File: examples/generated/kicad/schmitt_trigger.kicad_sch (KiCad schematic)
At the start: 6 parts

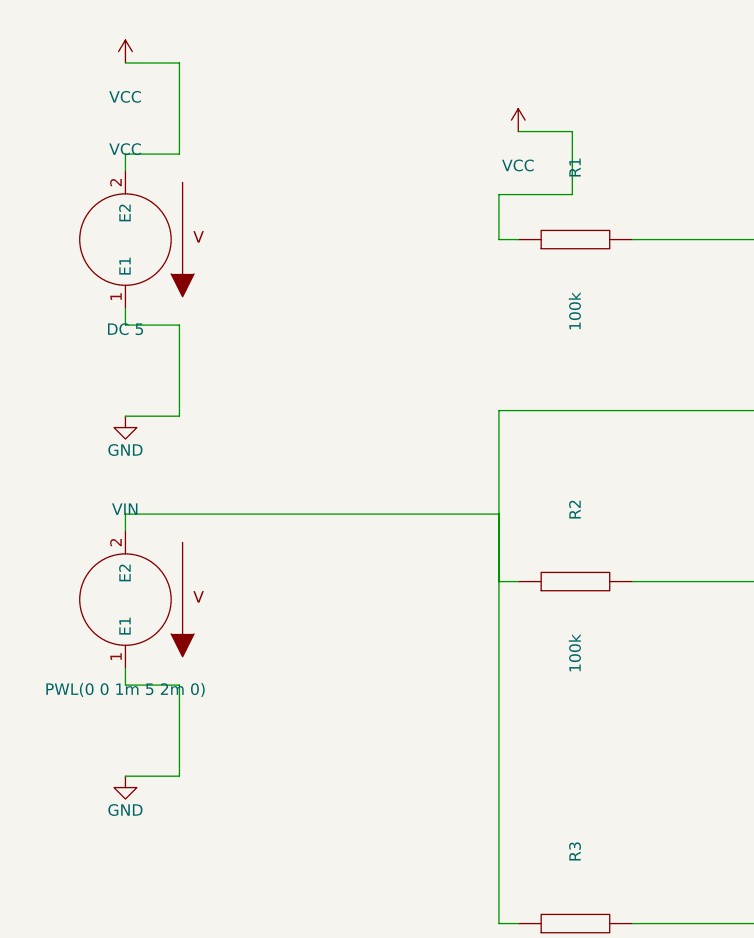
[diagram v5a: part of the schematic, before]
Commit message: Attempt to fix kinking and terminal direction issuses.
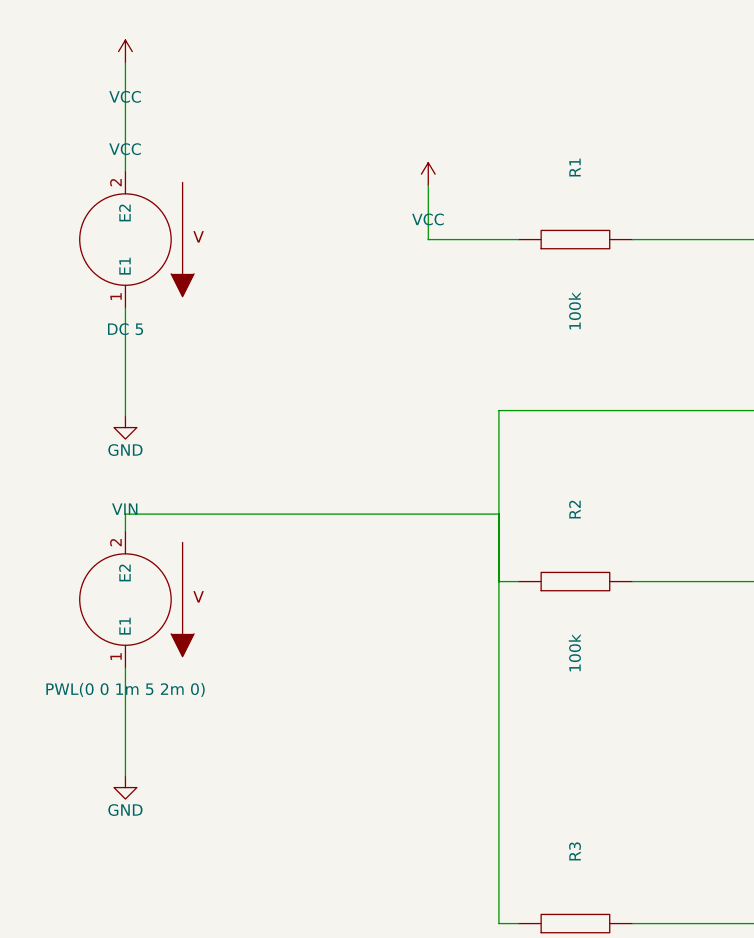
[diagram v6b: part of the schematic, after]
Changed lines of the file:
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@@
     )
   )
-  (symbol (lib_id "VCC") (at 93.65 58.00 0) (unit 1)
+  (symbol (lib_id "VCC") (at 83.65 64.00 0) (unit 1)
     (in_bom yes) (on_board yes)
-    (property "Reference" "#PWR0004" (at 93.65 54.19 0)
+    (property "Reference" "#PWR0004" (at 83.65 60.19 0)
       (effects (font (size 1.27 1.27)) hide)
     )
-    (property "Value" "VCC" (at 93.65 61.81 0)
+    (property "Value" "VCC" (at 83.65 67.81 0)
       (effects (font (size 1.27 1.27)))
     )
@@
     )
   )
-  (wire (pts (xy 50.00 62.38) (xy 50.00 60.50))
+  (wire (pts (xy 50.00 62.38) (xy 50.00 50.38))
     (stroke (width 0) (type solid) (color 0 0 0 0))
   )
-  (wire (pts (xy 50.00 60.50) (xy 56.00 60.50))
+  (wire (pts (xy 50.00 77.62) (xy 50.00 89.62))
     (stroke (width 0) (type solid) (color 0 0 0 0))
   )
-  (wire (pts (xy 56.00 60.50) (xy 56.00 50.38))
+  (wire (pts (xy 50.00 117.62) (xy 50.00 129.62))
     (stroke (width 0) (type solid) (color 0 0 0 0))
   )
-  (wire (pts (xy 56.00 50.38) (xy 50.00 50.38))
+  (wire (pts (xy 93.65 70.00) (xy 83.65 70.00))
     (stroke (width 0) (type solid) (color 0 0 0 0))
   )
-  (wire (pts (xy 50.00 77.62) (xy 50.00 79.50))
+  (wire (pts (xy 83.65 70.00) (xy 83.65 64.00))
     (stroke (width 0) (type solid) (color 0 0 0 0))
   )
-  (wire (pts (xy 50.00 79.50) (xy 56.00 79.50))
-    (stroke (width 0) (type solid) (color 0 0 0 0))
-  )
-  (wire (pts (xy 56.00 79.50) (xy 56.00 89.62))
-    (stroke (width 0) (type solid) (color 0 0 0 0))
-  )
-  (wire (pts (xy 56.00 89.62) (xy 50.00 89.62))
-    (stroke (width 0) (type solid) (color 0 0 0 0))
-  )
-  (wire (pts (xy 50.00 117.62) (xy 50.00 119.50))
-    (stroke (width 0) (type solid) (color 0 0 0 0))
-  )
-  (wire (pts (xy 50.00 119.50) (xy 56.00 119.50))
-    (stroke (width 0) (type solid) (color 0 0 0 0))
-  )
-  (wire (pts (xy 56.00 119.50) (xy 56.00 129.62))
-    (stroke (width 0) (type solid) (color 0 0 0 0))
-  )
-  (wire (pts (xy 56.00 129.62) (xy 50.00 129.62))
-    (stroke (width 0) (type solid) (color 0 0 0 0))
-  )
-  (wire (pts (xy 93.65 70.00) (xy 91.50 70.00))
-    (stroke (width 0) (type solid) (color 0 0 0 0))
-  )
-  (wire (pts (xy 91.50 70.00) (xy 91.50 65.00))
-    (stroke (width 0) (type solid) (color 0 0 0 0))
-  )
-  (wire (pts (xy 91.50 65.00) (xy 99.65 65.00))
-    (stroke (width 0) (type solid) (color 0 0 0 0))
-  )
-  (wire (pts (xy 99.65 65.00) (xy 99.65 58.00))
-    (stroke (width 0) (type solid) (color 0 0 0 0))
-  )
-  (wire (pts (xy 99.65 58.00) (xy 93.65 58.00))
-    (stroke (width 0) (type solid) (color 0 0 0 0))
-  )
